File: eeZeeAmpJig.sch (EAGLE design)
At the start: 18 parts

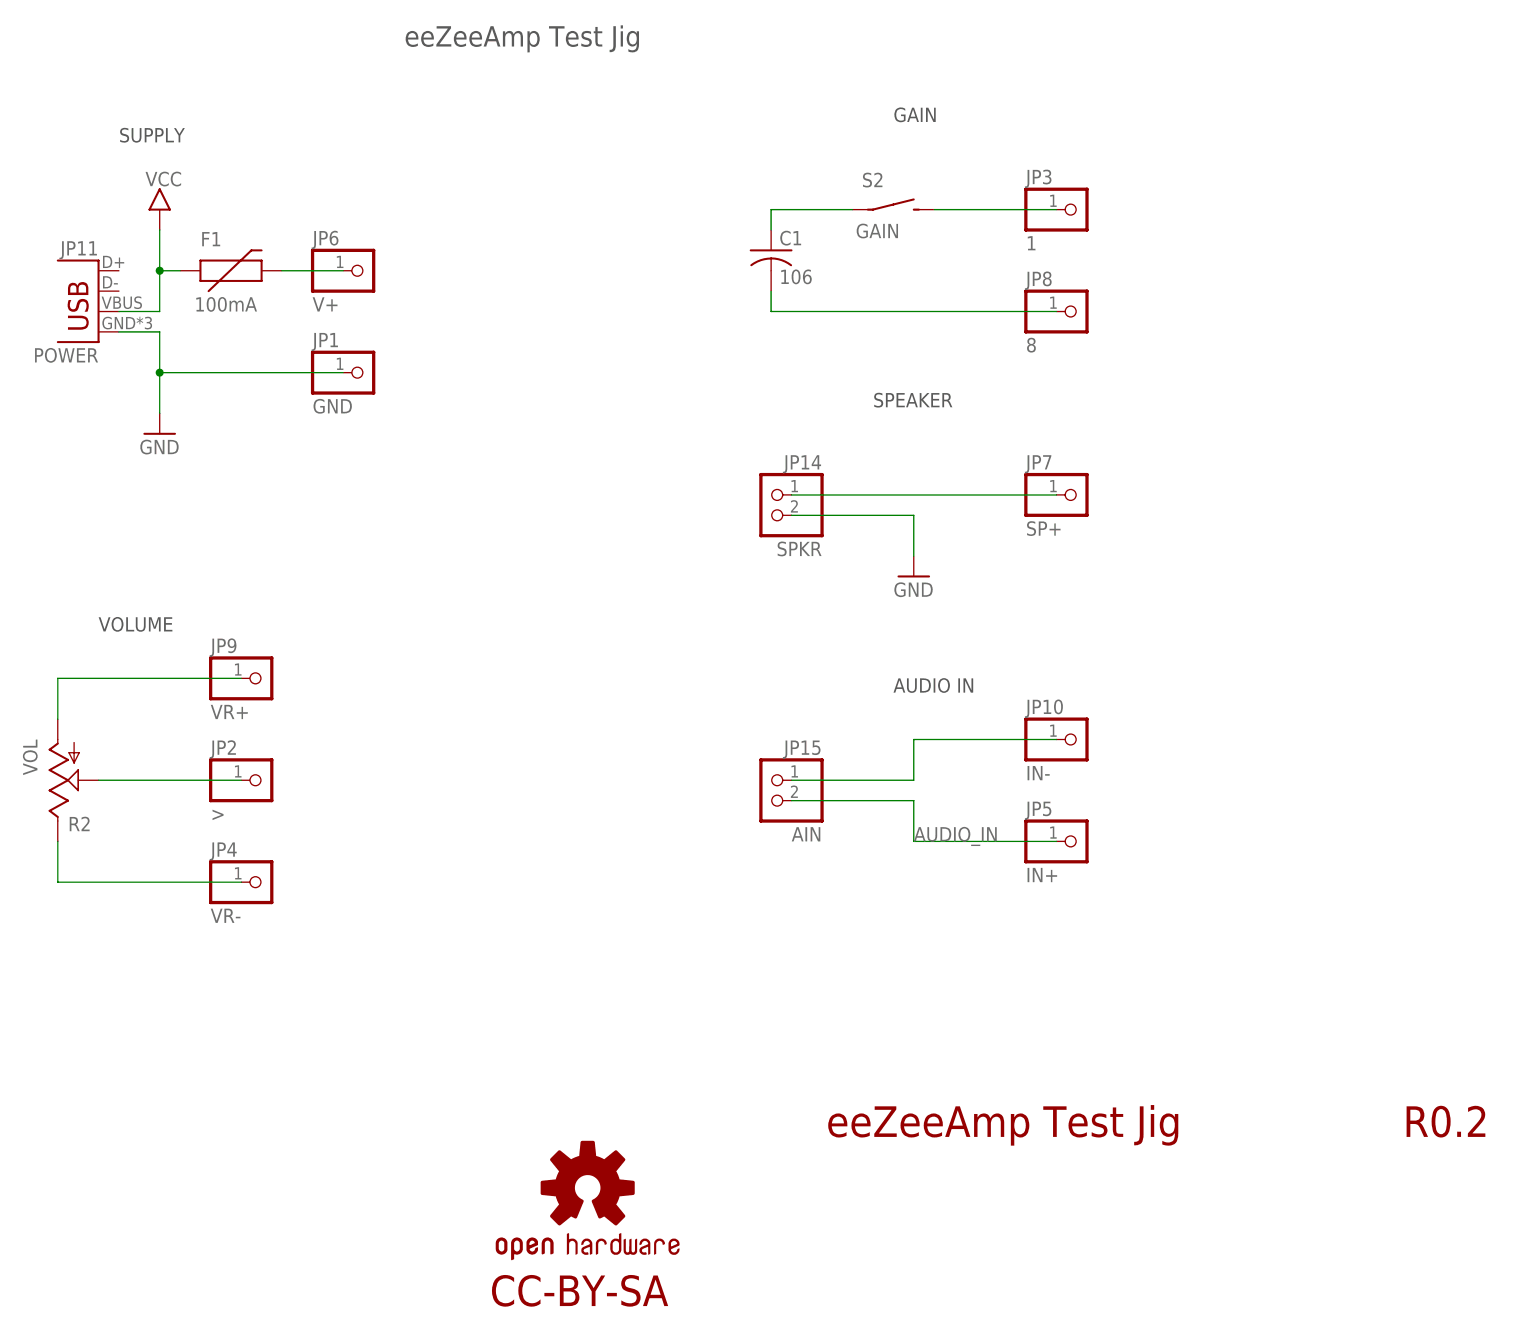
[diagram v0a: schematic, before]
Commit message: Altered gain to 40.5 with resistor, changed pot value, created silk and gerbers
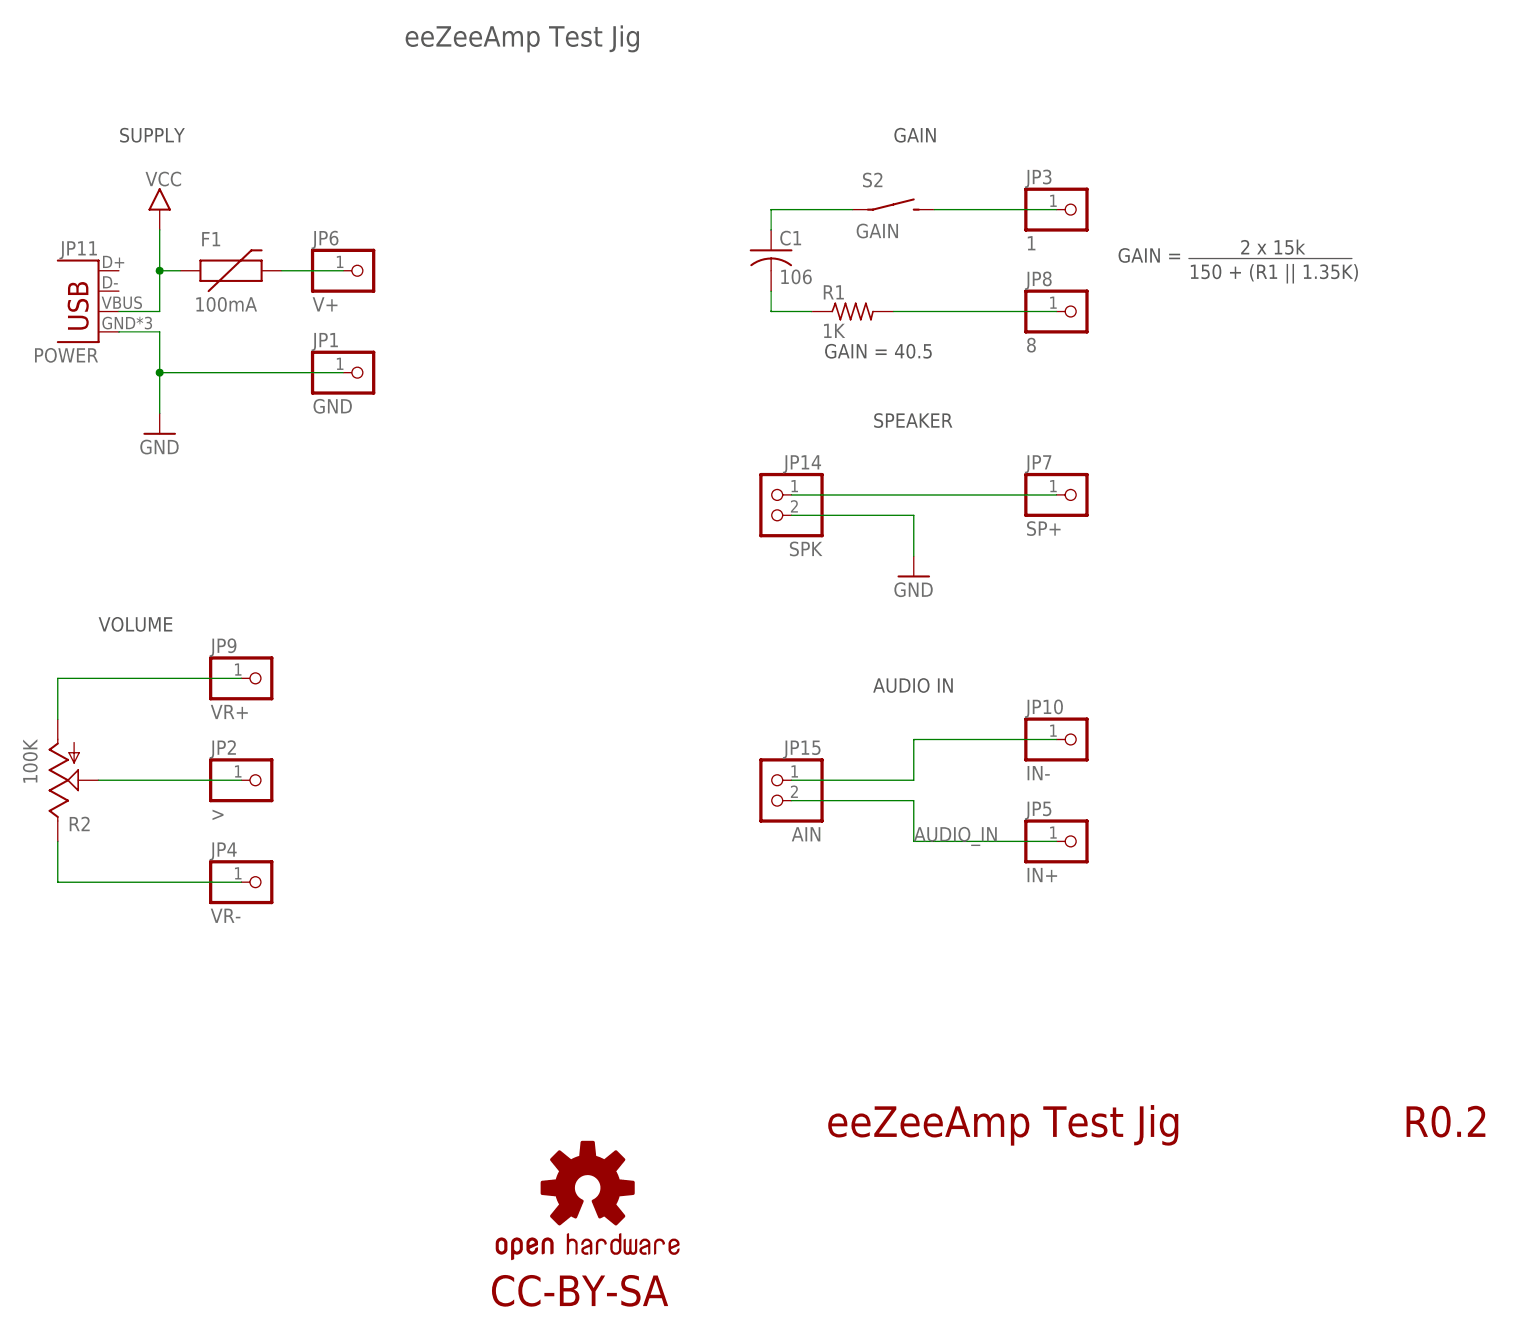
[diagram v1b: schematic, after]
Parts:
- added R1: 1K, rcl:R-US_R0603
- JP14: value SPKR -> SPK
- R2: value VOL -> 100K
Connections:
- new net N$5: C1.2, R1.1
- net 8: now also R1.2; no longer C1.2
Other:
- note added: "150 + (R1 || 1.35K)"
- note added: "2 x 15k"
- note added: "GAIN ="
- note added: "GAIN = 40.5"
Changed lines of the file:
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@@
 <setting verticaltext="up"/>
 </settings>
-<grid distance="0.1" unitdist="inch" unit="inch" style="lines" multiple="1" display="no" altdistance="0.01" altunitdist="inch" altunit="inch"/>
+<grid distance="0.01" unitdist="inch" unit="inch" style="lines" multiple="1" display="no" altdistance="0.01" altunitdist="inch" altunit="inch"/>
 <layers>
-<layer number="1" name="Top" color="4" fill="1" visible="yes" active="no"/>
-<layer number="16" name="Bottom" color="1" fill="1" visible="yes" active="no"/>
-<layer number="17" name="Pads" color="2" fill="1" visible="yes" active="no"/>
-<layer number="18" name="Vias" color="2" fill="1" visible="yes" active="no"/>
-<layer number="19" name="Unrouted" color="6" fill="1" visible="yes" active="no"/>
-<layer number="20" name="Dimension" color="15" fill="1" visible="yes" active="no"/>
-<layer number="21" name="tPlace" color="7" fill="1" visible="yes" active="no"/>
-<layer number="22" name="bPlace" color="7" fill="1" visible="yes" active="no"/>
-<layer number="23" name="tOrigins" color="15" fill="1" visible="yes" active="no"/>
-<layer number="24" name="bOrigins" color="15" fill="1" visible="yes" active="no"/>
-<layer number="25" name="tNames" color="7" fill="1" visible="yes" active="no"/>
-<layer number="26" name="bNames" color="7" fill="1" visible="yes" active="no"/>
-<layer number="27" name="tValues" color="7" fill="1" visible="yes" active="no"/>
-<layer number="28" name="bValues" color="7" fill="1" visible="yes" active="no"/>
+<layer number="1" name="Top" color="4" fill="1" visible="no" active="no"/>
+<layer number="16" name="Bottom" color="1" fill="1" visible="no" active="no"/>
+<layer number="17" name="Pads" color="2" fill="1" visible="no" active="no"/>
+<layer number="18" name="Vias" color="2" fill="1" visible="no" active="no"/>
+<layer number="19" name="Unrouted" color="6" fill="1" visible="no" active="no"/>
+<layer number="20" name="Dimension" color="15" fill="1" visible="no" active="no"/>
+<layer number="21" name="tPlace" color="7" fill="1" visible="no" active="no"/>
+<layer number="22" name="bPlace" color="7" fill="1" visible="no" active="no"/>
+<layer number="23" name="tOrigins" color="15" fill="1" visible="no" active="no"/>
+<layer number="24" name="bOrigins" color="15" fill="1" visible="no" active="no"/>
+<layer number="25" name="tNames" color="7" fill="1" visible="no" active="no"/>
+<layer number="26" name="bNames" color="7" fill="1" visible="no" active="no"/>
+<layer number="27" name="tValues" color="7" fill="1" visible="no" active="no"/>
+<layer number="28" name="bValues" color="7" fill="1" visible="no" active="no"/>
 <layer number="29" name="tStop" color="7" fill="3" visible="no" active="no"/>
 <layer number="30" name="bStop" color="7" fill="6" visible="no" active="no"/>
@@
 <layer number="35" name="tGlue" color="7" fill="4" visible="no" active="no"/>
 <layer number="36" name="bGlue" color="7" fill="5" visible="no" active="no"/>
-<layer number="37" name="tTest" color="7" fill="1" visible="yes" active="no"/>
-<layer number="38" name="bTest" color="7" fill="1" visible="yes" active="no"/>
+<layer number="37" name="tTest" color="7" fill="1" visible="no" active="no"/>
+<layer number="38" name="bTest" color="7" fill="1" visible="no" active="no"/>
 <layer number="39" name="tKeepout" color="4" fill="11" visible="no" active="no"/>
 <layer number="40" name="bKeepout" color="1" fill="11" visible="no" active="no"/>
@@
 <layer number="44" name="Drills" color="7" fill="1" visible="no" active="no"/>
 <layer number="45" name="Holes" color="7" fill="1" visible="no" active="no"/>
-<layer number="46" name="Milling" color="3" fill="1" visible="yes" active="no"/>
-<layer number="47" name="Measures" color="7" fill="1" visible="yes" active="no"/>
-<layer number="48" name="Document" color="7" fill="1" visible="yes" active="no"/>
-<layer number="49" name="Reference" color="7" fill="1" visible="yes" active="no"/>
-<layer number="50" name="dxf" color="7" fill="1" visible="yes" active="no"/>
-<layer number="51" name="tDocu" color="7" fill="1" visible="yes" active="no"/>
-<layer number="52" name="bDocu" color="7" fill="1" visible="yes" active="no"/>
-<layer number="53" name="tPadExt" color="7" fill="1" visible="yes" active="no"/>
-<layer number="54" name="bPadExt" color="1" fill="1" visible="yes" active="no"/>
-<layer number="56" name="wert" color="7" fill="1" visible="yes" active="no"/>
-<layer number="57" name="tCAD" color="7" fill="1" visible="yes" active="no"/>
-<layer number="59" name="tCarbon" color="7" fill="1" visible="yes" active="no"/>
-<layer number="60" name="bCarbon" color="7" fill="1" visible="yes" active="no"/>
+<layer number="46" name="Milling" color="3" fill="1" visible="no" active="no"/>
+<layer number="47" name="Measures" color="7" fill="1" visible="no" active="no"/>
+<layer number="48" name="Document" color="7" fill="1" visible="no" active="no"/>
+<layer number="49" name="Reference" color="7" fill="1" visible="no" active="no"/>
+<layer number="50" name="dxf" color="7" fill="1" visible="no" active="no"/>
+<layer number="51" name="tDocu" color="7" fill="1" visible="no" active="no"/>
+<layer number="52" name="bDocu" color="7" fill="1" visible="no" active="no"/>
+<layer number="53" name="tPadExt" color="7" fill="1" visible="no" active="no"/>
+<layer number="54" name="bPadExt" color="1" fill="1" visible="no" active="no"/>
+<layer number="56" name="wert" color="7" fill="1" visible="no" active="no"/>
+<layer number="57" name="tCAD" color="7" fill="1" visible="no" active="no"/>
+<layer number="59" name="tCarbon" color="7" fill="1" visible="no" active="no"/>
+<layer number="60" name="bCarbon" color="7" fill="1" visible="no" active="no"/>
 <layer number="90" name="Modules" color="5" fill="1" visible="yes" active="yes"/>
 <layer number="91" name="Nets" color="2" fill="1" visible="yes" active="yes"/>
@@
 <part name="JP10" library="pinhead-2" deviceset="PINHD-1X01" device="_2.54-S" value="IN-"/>
 <part name="LOGO2" library="SparkFun-Aesthetics" deviceset="OSHW-LOGO" device="S"/>
-<part name="R2" library="pot" deviceset="TRIM_US-" device="CA6H" value="VOL"/>
+<part name="R2" library="pot" deviceset="TRIM_US-" device="CA6H" value="100K"/>
 <part name="C1" library="rcl" deviceset="C-US" device="C1206" value="106"/>
 <part name="GND3" library="bt" deviceset="GND" device=""/>
@@
 <part name="U$2" library="bt" deviceset="VCC" device="" value=""/>
 <part name="S2" library="bt_electromech" deviceset="SPST" device="_TAC_RECT1" value="GAIN"/>
-<part name="JP14" library="pinhead-2" deviceset="PINHD-1X02" device="_2.54-S" value="SPKR"/>
+<part name="JP14" library="pinhead-2" deviceset="PINHD-1X02" device="_2.54-S" value="SPK"/>
 <part name="JP15" library="pinhead-2" deviceset="PINHD-1X02" device="_2.54-S" value="AIN"/>
 <part name="F1" library="bt" deviceset="PTC" device="0603" value="100mA"/>
 <part name="JP11" library="SparkFun-Connectors" deviceset="USB" device="-MICROB" value="POWER"/>
+<part name="R1" library="rcl" deviceset="R-US_" device="R0603" value="1K"/>
 </parts>
 <sheets>
@@
 <text x="231.14" y="24.13" size="3.81" layer="94">R0.2</text>
 <text x="106.68" y="160.02" size="2.54" layer="97">eeZeeAmp Test Jig</text>
-<text x="167.64" y="150.622" size="1.778" layer="97">GAIN</text>
+<text x="167.64" y="148.082" size="1.778" layer="97">GAIN</text>
 <text x="117.348" y="3.048" size="3.81" layer="94" ratio="20">CC-BY-SA</text>
 <text x="68.58" y="87.122" size="1.778" layer="97">VOLUME</text>
 <text x="71.12" y="148.082" size="1.778" layer="97">SUPPLY</text>
-<text x="167.64" y="79.502" size="1.778" layer="97">AUDIO IN</text>
-<text x="165.1" y="115.062" size="1.778" layer="97">SPEAKER</text>
+<text x="165.1" y="79.502" size="1.778" layer="97">AUDIO IN</text>
+<text x="165.1" y="112.522" size="1.778" layer="97">SPEAKER</text>
+<text x="195.58" y="133.096" size="1.778" layer="97">GAIN = </text>
+<text x="210.82" y="134.112" size="1.778" layer="97">2 x 15k</text>
+<text x="204.47" y="131.064" size="1.778" layer="97">150 + (R1 || 1.35K)</text>
+<wire x1="204.47" y1="133.604" x2="224.79" y2="133.604" width="0.1524" layer="97"/>
+<text x="159.004" y="121.158" size="1.778" layer="97">GAIN = 40.5</text>
 </plain>
 <instances>
@@
 <instance part="F1" gate="G$1" x="83.82" y="132.08"/>
 <instance part="JP11" gate="G$1" x="68.58" y="124.46" rot="MR0"/>
+<instance part="R1" gate="G$1" x="162.56" y="127"/>
 </instances>
 <busses>
@@
 <net name="8" class="0">
 <segment>
-<wire x1="152.4" y1="129.54" x2="152.4" y2="127" width="0.1524" layer="91"/>
-<wire x1="152.4" y1="127" x2="187.96" y2="127" width="0.1524" layer="91"/>
 <pinref part="JP8" gate="A" pin="1"/>
-<pinref part="C1" gate="G$1" pin="2"/>
+<pinref part="R1" gate="G$1" pin="2"/>
+<wire x1="167.64" y1="127" x2="187.96" y2="127" width="0.1524" layer="91"/>
 </segment>
 </net>
@@
 </segment>
 </net>
+<net name="N$5" class="0">
+<segment>
+<pinref part="R1" gate="G$1" pin="1"/>
+<pinref part="C1" gate="G$1" pin="2"/>
+<wire x1="152.4" y1="129.54" x2="152.4" y2="127" width="0.1524" layer="91"/>
+<wire x1="152.4" y1="127" x2="157.48" y2="127" width="0.1524" layer="91"/>
+</segment>
+</net>

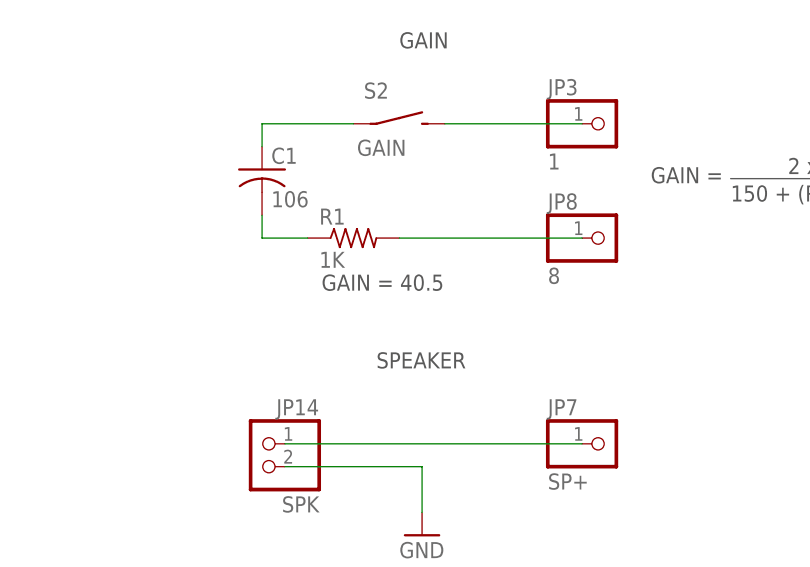
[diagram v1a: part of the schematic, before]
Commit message: Added test jig schematic
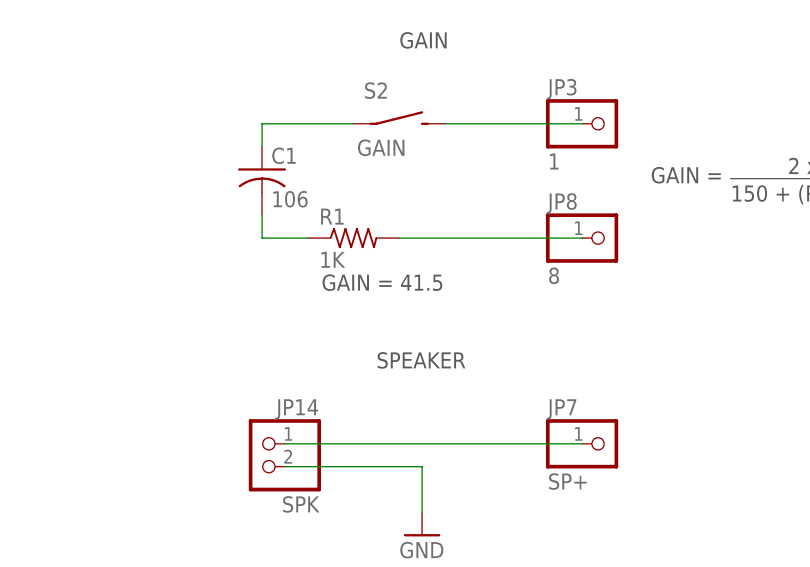
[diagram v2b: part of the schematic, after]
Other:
- note added: "GAIN = 41.5"
- note removed: "GAIN = 40.5"
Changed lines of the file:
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@@
 <text x="204.47" y="131.064" size="1.778" layer="97">150 + (R1 || 1.35K)</text>
 <wire x1="204.47" y1="133.604" x2="224.79" y2="133.604" width="0.1524" layer="97"/>
-<text x="159.004" y="121.158" size="1.778" layer="97">GAIN = 40.5</text>
+<text x="159.004" y="121.158" size="1.778" layer="97">GAIN = 41.5</text>
 </plain>
 <instances>
